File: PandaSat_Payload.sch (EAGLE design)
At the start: 16 parts, among them J1 U.FL, J5 U.FL, J6 FEMALE 2x3, U1 CH340G, U12 EP2W+, U14 S1216V8, Y1 12MHz

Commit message: Adding last version of Panda_Payload PCB
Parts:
- removed X3: (no value), con-berg:PN87520
- added J2: (no value), SparkFun-Connectors:CONN_04
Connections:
- net ENABLE renamed ENABLE1
- removed net N$10: X3.3
- removed net N$8: U1.UD-, X3.2
- removed net N$9: U1.UD+, X3.1
- removed net SHLD: X3.4
- new net ENABLE2: J6.5
- new net GPS_CLK: PCB1.GPIO24, U14.1PPS
- new net UD+: J2.2, U1.UD+
- new net UD-: J2.3, U1.UD-
- net GND: now also J2.1
- net VCC3.3: no longer J6.5
- net VCC5: now also J2.4
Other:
- note added: "FTDI : USB (Pi) to Serial (GPS Receiver)"
- note removed: "USB to Serial (FTDI)"
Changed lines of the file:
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@@
 <part name="C8" library="SparkFun-Capacitors" deviceset="0.1UF-25V(+80/-20%)(0603)" device="" value="0.1uF"/>
 <part name="SUPPLY1" library="SparkFun-Aesthetics" deviceset="VCC" device=""/>
-<part name="X3" library="con-berg" library_urn="urn:adsk.eagle:library:130" deviceset="PN87520" device="" package3d_urn="urn:adsk.eagle:package:6146/1"/>
 <part name="FRAME1" library="SparkFun-Aesthetics" deviceset="FRAME-LETTER" device="NO_PACKAGE"/>
 <part name="FRAME2" library="SparkFun-Aesthetics" deviceset="FRAME-LETTER" device="NO_PACKAGE"/>
+<part name="J2" library="SparkFun-Connectors" deviceset="CONN_04" device=""/>
 </parts>
 <sheets>
 <sheet>
+<description>GPS and Single Board Computer</description>
 <plain>
 <wire x1="147.32" y1="35.56" x2="147.32" y2="78.74" width="0.1524" layer="95" style="longdash"/>
@@
 </segment>
 <segment>
-<pinref part="J6" gate="G$1" pin="5"/>
-<wire x1="185.42" y1="55.88" x2="172.72" y2="55.88" width="0.1524" layer="91"/>
-<label x="167.64" y="55.88" size="1.016" layer="95" xref="yes"/>
-</segment>
-<segment>
 <pinref part="PCB1" gate="G$1" pin="3V3@1"/>
 <wire x1="78.74" y1="162.56" x2="78.74" y2="175.26" width="0.1524" layer="91"/>
@@
 </segment>
 </net>
-<net name="ENABLE" class="0">
+<net name="D-" class="0">
+<segment>
+<pinref part="X1" gate="G$1" pin="3"/>
+<wire x1="121.92" y1="35.56" x2="134.62" y2="35.56" width="0.1524" layer="91"/>
+<label x="134.62" y="35.56" size="1.4224" layer="95" xref="yes"/>
+</segment>
+</net>
+<net name="D+" class="0">
+<segment>
+<pinref part="X1" gate="G$1" pin="2"/>
+<wire x1="121.92" y1="33.02" x2="134.62" y2="33.02" width="0.1524" layer="91"/>
+<label x="134.62" y="33.02" size="1.4224" layer="95" xref="yes"/>
+</segment>
+</net>
+<net name="ENABLE2" class="0">
+<segment>
+<pinref part="J6" gate="G$1" pin="5"/>
+<wire x1="185.42" y1="55.88" x2="172.72" y2="55.88" width="0.1524" layer="91"/>
+<label x="167.64" y="55.88" size="1.016" layer="95" xref="yes"/>
+</segment>
+</net>
+<net name="GPS_CLK" class="0">
+<segment>
+<pinref part="U14" gate="G$1" pin="1PPS"/>
+<wire x1="210.82" y1="144.78" x2="226.06" y2="144.78" width="0.1524" layer="91"/>
+<label x="226.06" y="144.78" size="1.4224" layer="95" xref="yes"/>
+</segment>
+<segment>
+<pinref part="PCB1" gate="G$1" pin="GPIO24"/>
+<wire x1="106.68" y1="121.92" x2="132.08" y2="121.92" width="0.1524" layer="91"/>
+<label x="132.08" y="121.92" size="1.4224" layer="95" xref="yes"/>
+</segment>
+</net>
+<net name="ENABLE1" class="0">
 <segment>
 <pinref part="J6" gate="G$1" pin="6"/>
@@
 </segment>
 </net>
-<net name="D-" class="0">
-<segment>
-<pinref part="X1" gate="G$1" pin="3"/>
-<wire x1="121.92" y1="35.56" x2="134.62" y2="35.56" width="0.1524" layer="91"/>
-<label x="134.62" y="35.56" size="1.4224" layer="95" xref="yes"/>
-</segment>
-</net>
-<net name="D+" class="0">
-<segment>
-<pinref part="X1" gate="G$1" pin="2"/>
-<wire x1="121.92" y1="33.02" x2="134.62" y2="33.02" width="0.1524" layer="91"/>
-<label x="134.62" y="33.02" size="1.4224" layer="95" xref="yes"/>
-</segment>
-</net>
 </nets>
 </sheet>
 <sheet>
+<description>Interface USB-UART</description>
 <plain>
 <wire x1="0" y1="129.54" x2="71.12" y2="129.54" width="0.1524" layer="95" style="longdash"/>
 <wire x1="71.12" y1="129.54" x2="248.92" y2="129.54" width="0.1524" layer="95" style="longdash"/>
 <wire x1="71.12" y1="185.42" x2="71.12" y2="129.54" width="0.1524" layer="95" style="longdash"/>
-<text x="114.3" y="137.16" size="2.54" layer="97">USB to Serial (FTDI)</text>
+<text x="114.3" y="137.16" size="2.54" layer="97">FTDI : USB (Pi) to Serial (GPS Receiver)</text>
 </plain>
 <instances>
@@
 <instance part="SUPPLY1" gate="G$1" x="226.06" y="177.8" smashed="yes">
 <attribute name="VALUE" x="225.044" y="181.356" size="1.778" layer="96"/>
-</instance>
-<instance part="X3" gate="G$1" x="91.44" y="167.64" smashed="yes" rot="R180">
-<attribute name="NAME" x="91.44" y="156.21" size="1.778" layer="95"/>
-<attribute name="VALUE" x="91.44" y="175.26" size="1.778" layer="96" rot="R180"/>
 </instance>
 <instance part="FRAME2" gate="G$1" x="0" y="0" smashed="yes"/>
@@
 <attribute name="DRAWING_NAME" x="162.814" y="17.78" size="2.7432" layer="94" font="vector"/>
 <attribute name="DESIGNER" x="170.434" y="11.176" size="2.7432" layer="94" font="vector"/>
+</instance>
+<instance part="J2" gate="G$1" x="88.9" y="162.56" smashed="yes">
+<attribute name="VALUE" x="83.82" y="155.194" size="1.778" layer="96" font="vector"/>
+<attribute name="NAME" x="83.82" y="170.688" size="1.778" layer="95" font="vector"/>
 </instance>
 </instances>
@@
 <wire x1="187.96" y1="144.78" x2="187.96" y2="147.32" width="0.1524" layer="91"/>
 </segment>
+<segment>
+<pinref part="J2" gate="G$1" pin="1"/>
+<wire x1="93.98" y1="160.02" x2="101.6" y2="160.02" width="0.1524" layer="91"/>
+<label x="101.6" y="160.02" size="1.016" layer="95" xref="yes"/>
+</segment>
 </net>
 <net name="TXO" class="0">
@@
 </segment>
 </net>
-<net name="N$8" class="0">
-<segment>
-<wire x1="93.98" y1="165.1" x2="160.02" y2="165.1" width="0.1524" layer="91"/>
+<net name="UD-" class="0">
+<segment>
 <wire x1="160.02" y1="165.1" x2="162.56" y2="162.56" width="0.1524" layer="91"/>
 <pinref part="U1" gate="U1" pin="UD-"/>
 <wire x1="162.56" y1="162.56" x2="193.04" y2="162.56" width="0.1524" layer="91"/>
-<pinref part="X3" gate="G$1" pin="2"/>
-</segment>
-</net>
-<net name="N$9" class="0">
+<pinref part="J2" gate="G$1" pin="3"/>
+<wire x1="160.02" y1="165.1" x2="93.98" y2="165.1" width="0.1524" layer="91"/>
+<label x="101.6" y="165.1" size="1.016" layer="95"/>
+</segment>
+</net>
+<net name="UD+" class="0">
 <segment>
 <wire x1="93.98" y1="162.56" x2="160.02" y2="162.56" width="0.1524" layer="91"/>
@@
 <pinref part="U1" gate="U1" pin="UD+"/>
 <wire x1="162.56" y1="165.1" x2="193.04" y2="165.1" width="0.1524" layer="91"/>
-<pinref part="X3" gate="G$1" pin="1"/>
+<pinref part="J2" gate="G$1" pin="2"/>
+<label x="101.6" y="162.56" size="1.016" layer="95"/>
 </segment>
 </net>
@@
 </segment>
 </net>
-<net name="SHLD" class="0">
-<segment>
-<label x="114.3" y="170.18" size="1.27" layer="95" xref="yes"/>
-<pinref part="X3" gate="G$1" pin="4"/>
-<wire x1="114.3" y1="170.18" x2="93.98" y2="170.18" width="0.1524" layer="91"/>
-</segment>
-</net>
-<net name="N$10" class="0">
-<segment>
-<wire x1="93.98" y1="167.64" x2="121.92" y2="167.64" width="0.1524" layer="91"/>
-<wire x1="121.92" y1="167.64" x2="121.92" y2="175.26" width="0.1524" layer="91"/>
-<pinref part="X3" gate="G$1" pin="3"/>
-</segment>
-</net>
+<net name="VCC5" class="0">
+<segment>
+<pinref part="J2" gate="G$1" pin="4"/>
+<wire x1="93.98" y1="167.64" x2="101.6" y2="167.64" width="0.1524" layer="91"/>
+<label x="101.6" y="167.64" size="1.016" layer="95" xref="yes"/>
+</segment>
+</net>

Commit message: Added Last version of PandaSat_Payload sch/board
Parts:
- added J3: (no value), SparkFun-Connectors:CONN_04
- added J4: FEMALE 2x3, SparkFun-Connectors:CONN_03X2FEMALE
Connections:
- removed net ENABLE2: J6.5
- removed net GPS_ANTENNA_1: J1.GND
- removed net GPS_ANTENNA_2: J5.GND
- removed net VCC: C8.1, U1.VCC
- new net D2+: J3.2, J4.5
- new net D2-: J3.3, J4.3
- net ENABLE1: now also J6.2; no longer J6.6
- net GND: now also J1.GND, J3.1, J4.1, J4.2, J4.4, J5.GND, J6.3; no longer J6.1
- net UART2_RX: now also J6.6; no longer J6.2
- net VCC5: now also C8.1, J3.4, J4.6, J6.1, U1.VCC; no longer J6.3
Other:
- note added: "Mother Board connector"

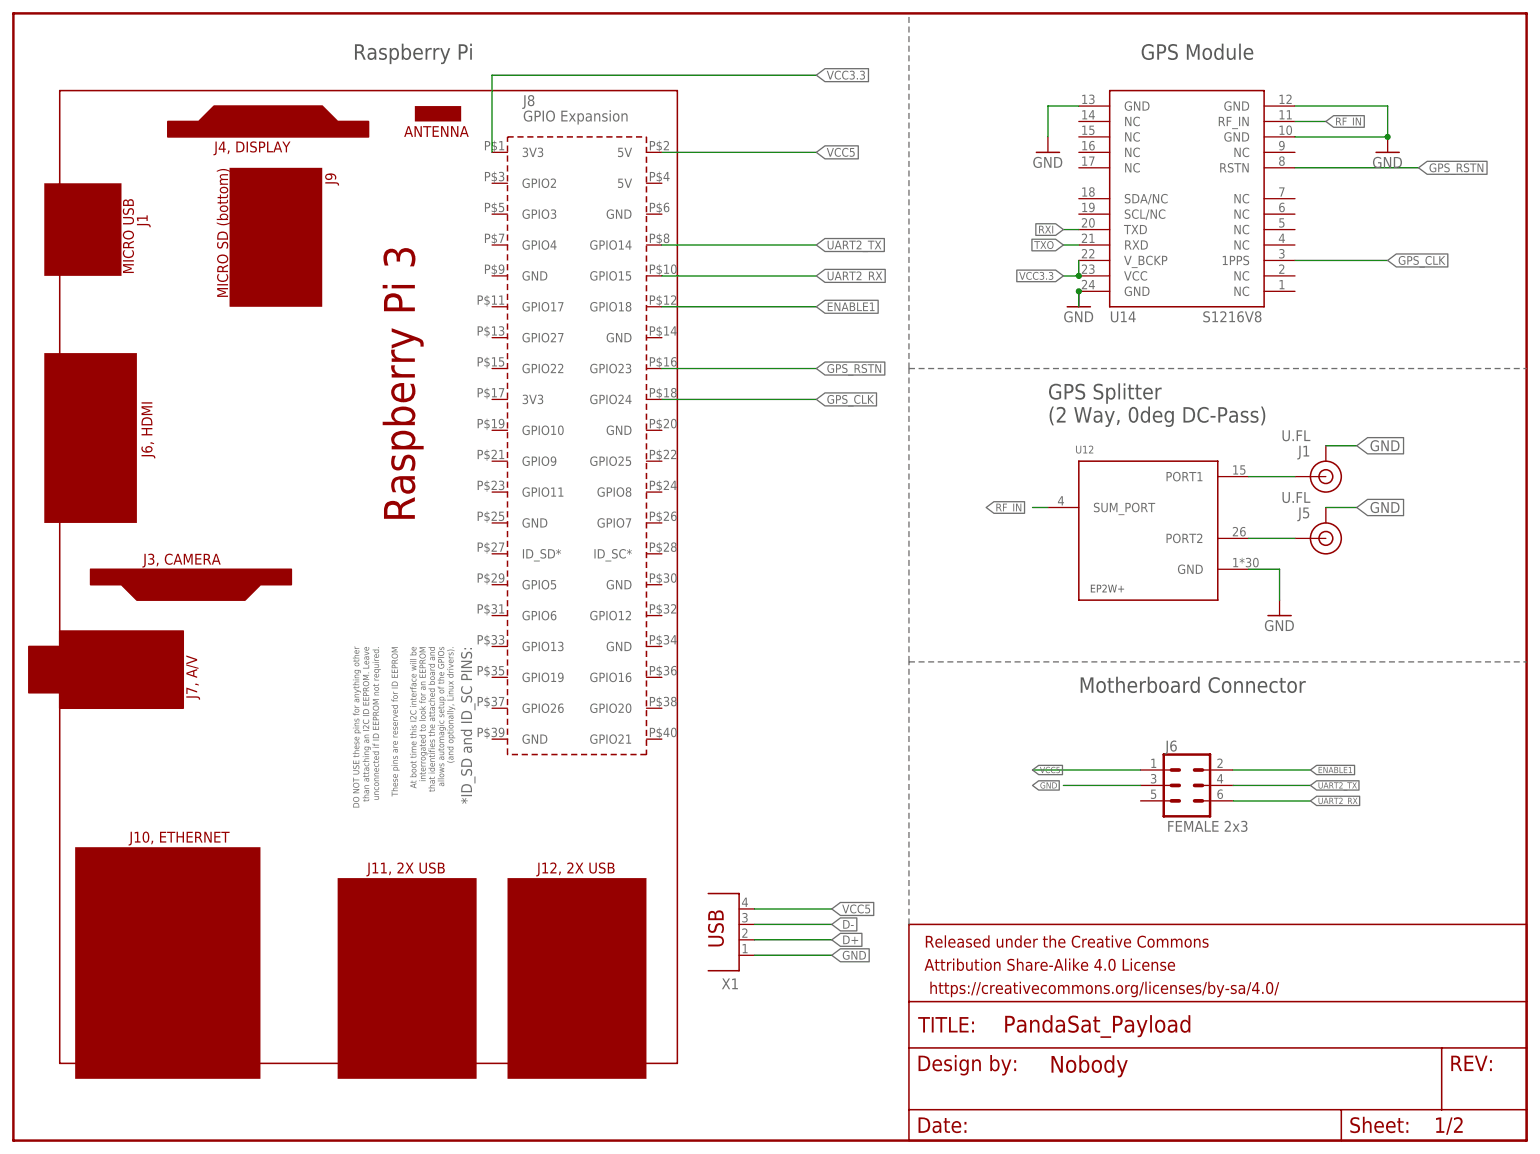
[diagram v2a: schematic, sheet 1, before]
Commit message: Added changes to the EAGLE files on the board
changed position of the SDR USB socket
changed the position of the USB 4 pins connector (closer to the Pi holes)
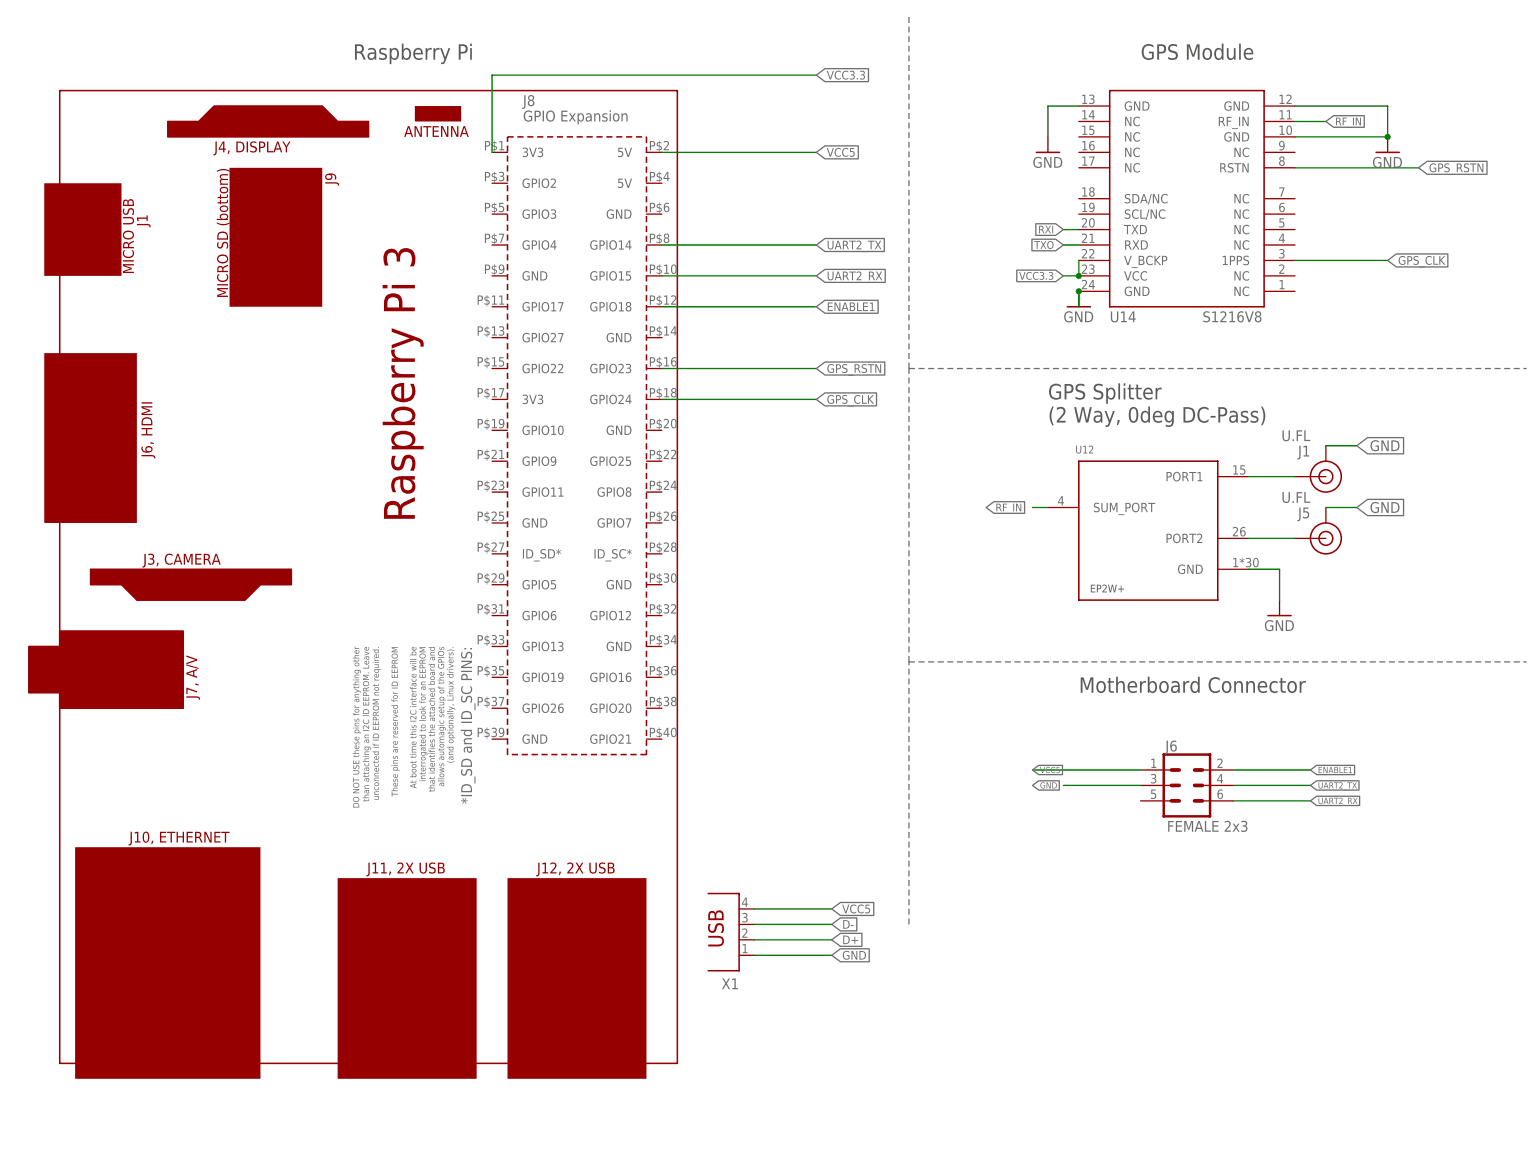
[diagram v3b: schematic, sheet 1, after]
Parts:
- removed FRAME1, FRAME2: FRAME-LETTERNO_PACKAGE, SparkFun-Aesthetics:FRAME-LETTERNO_PACKAGE
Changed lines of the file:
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@@
 <part name="GND9" library="SparkFun" deviceset="GND" device=""/>
 <part name="C8" library="SparkFun-Capacitors" deviceset="0.1UF-25V(+80/-20%)(0603)" device="" value="0.1uF"/>
-<part name="FRAME1" library="SparkFun-Aesthetics" deviceset="FRAME-LETTER" device="NO_PACKAGE"/>
-<part name="FRAME2" library="SparkFun-Aesthetics" deviceset="FRAME-LETTER" device="NO_PACKAGE"/>
 <part name="J2" library="SparkFun-Connectors" deviceset="CONN_04" device=""/>
 <part name="J3" library="SparkFun-Connectors" deviceset="CONN_04" device=""/>
@@
 <attribute name="VALUE" x="119.38" y="43.18" size="1.778" layer="96" rot="R180"/>
 </instance>
-<instance part="FRAME1" gate="G$1" x="0" y="0" smashed="yes"/>
-<instance part="FRAME1" gate="V" x="147.32" y="0" smashed="yes">
-<attribute name="LAST_DATE_TIME" x="160.02" y="1.27" size="2.54" layer="94" font="vector"/>
-<attribute name="SHEET" x="233.68" y="1.27" size="2.54" layer="94" font="vector"/>
-<attribute name="DRAWING_NAME" x="162.814" y="17.78" size="2.7432" layer="94" font="vector"/>
-<attribute name="DESIGNER" x="170.434" y="11.176" size="2.7432" layer="94" font="vector"/>
-</instance>
 </instances>
 <busses>
@@
 <attribute name="VALUE" x="227.584" y="165.481" size="1.778" layer="96"/>
 </instance>
-<instance part="FRAME2" gate="G$1" x="0" y="0" smashed="yes"/>
-<instance part="FRAME2" gate="V" x="147.32" y="0" smashed="yes">
-<attribute name="LAST_DATE_TIME" x="160.02" y="1.27" size="2.54" layer="94" font="vector"/>
-<attribute name="SHEET" x="233.68" y="1.27" size="2.54" layer="94" font="vector"/>
-<attribute name="DRAWING_NAME" x="162.814" y="17.78" size="2.7432" layer="94" font="vector"/>
-<attribute name="DESIGNER" x="170.434" y="11.176" size="2.7432" layer="94" font="vector"/>
-</instance>
 <instance part="J2" gate="G$1" x="88.9" y="162.56" smashed="yes">
